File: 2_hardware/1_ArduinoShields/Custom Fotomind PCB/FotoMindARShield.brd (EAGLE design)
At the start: 160 x 100 mm, 22 parts

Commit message: Last lines PCB Shield
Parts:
- moved R3 26.5 mm to (17.1, 31.8)
- moved CAMERA 11.9 mm to (18.1, 8.26)
- moved R4 10.8 mm to (8.26, 8.89), turned to 270 degrees
- moved R7 9.94 mm to (45.1, 37.8), turned to 90 degrees
- moved LED1 8.89 mm to (11.4, 22.9)
- moved LED2 8.89 mm to (5.08, 22.9)
- moved R5 3.81 mm to (5.08, 8.89), turned to 270 degrees
- moved R6 2.54 mm to (61.0, 36.8)
- moved R2 1.59 mm to (48.3, 37.8)
- moved R1 1.00 mm to (51.1, 37.8)
- turned EXTSENSOR to 180 degrees
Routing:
- net N$8: track 0.00 -> 135.3 mm
- net N$7: track 7.62 -> 121.0 mm
- net N$30: track 0.00 -> 75.9 mm
- net N$19: track 27.6 -> 87.4 mm
- net N$1: track 0.00 -> 58.0 mm
- net N$15: track 0.00 -> 54.5 mm
- net N$21: track 21.9 -> 76.4 mm
- net GND: track 61.7 -> 110.2 mm
- net N$14: track 0.00 -> 46.7 mm
- net N$13: track 0.00 -> 46.4 mm
- net N$28: track 0.00 -> 28.6 mm
- net N$26: track 0.00 -> 24.8 mm
- net N$2: track 0.00 -> 20.6 mm
- net N$5: track 0.00 -> 13.9 mm
- net N$20: track 0.00 -> 9.88 mm
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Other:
- board size 160 x 100 mm -> 73.6 x 59.4 mm

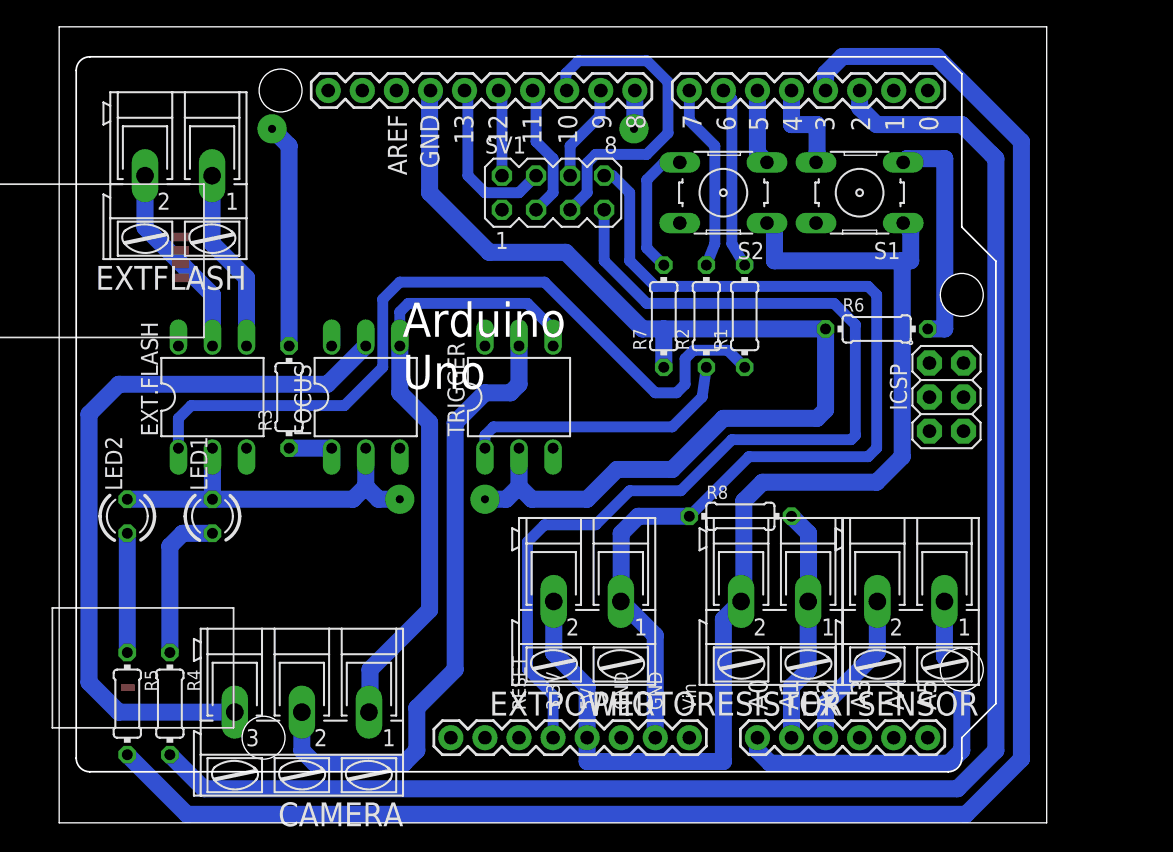
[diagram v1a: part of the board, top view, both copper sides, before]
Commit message: New ultrasonic feature
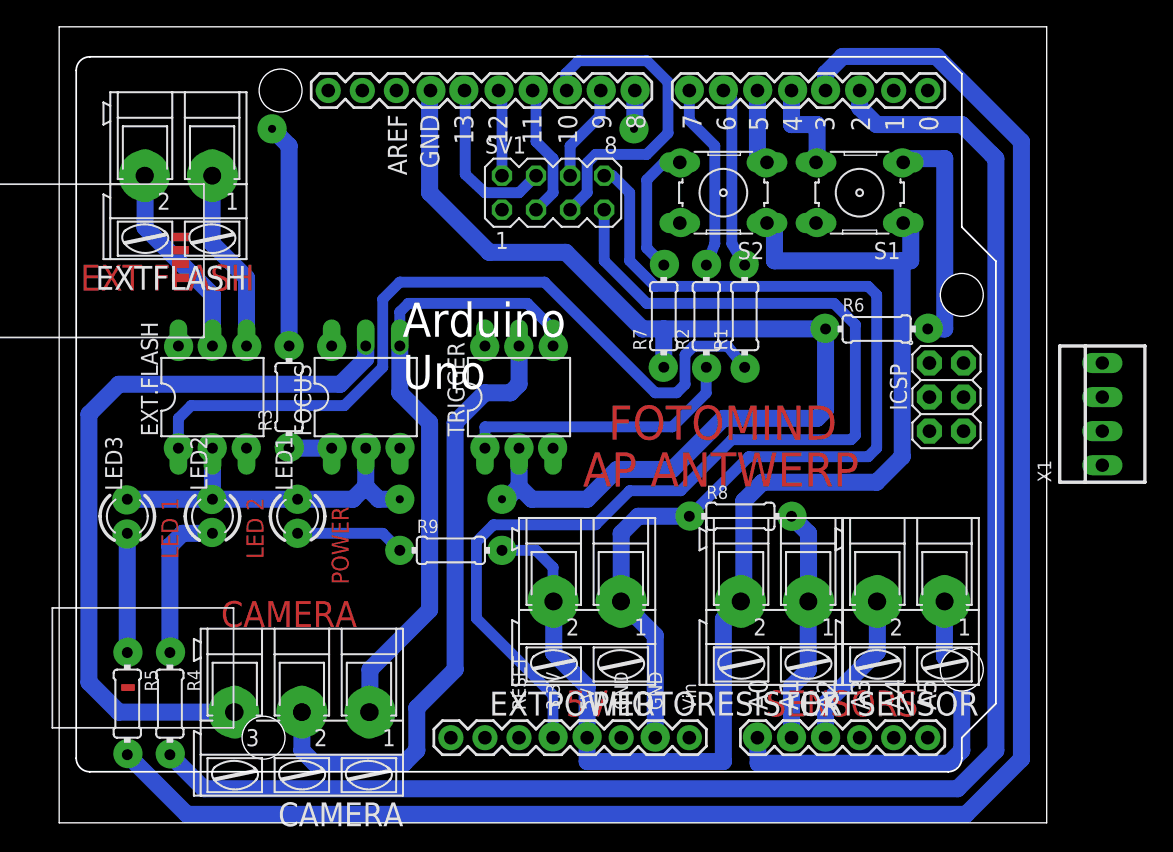
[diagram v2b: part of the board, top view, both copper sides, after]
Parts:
- added LED3: (no value), led:LED3MM
- added R9: 1k, eagle-ltspice:0204/7
- added X1: ULTRASOON, con-molex:22-23-2041
- S1: value (none) -> Trigger
- S2: value (none) -> Flash
- SV1: value (none) -> Wireless nRF24
- moved LED1 6.35 mm to (17.8, 22.9)
- moved LED2 6.35 mm to (11.4, 22.9)
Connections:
- removed net N$19: EXTPOWER.2, PCB1.5V, PHOTORESISTOR.2, S1.1, S2.1
- new net N$105: PCB1.0, X1.3
- new net N$107: PCB1.1, X1.2
- new net N$79: EXTPOWER.2, PCB1.5V, PHOTORESISTOR.2, R9.2, S1.1, S2.1, X1.4
- new net N$92: LED1.A, R9.1
- net GND: now also LED3.K
- net N$10: now also LED2.A; no longer LED1.A
- net N$21: now also X1.1
- net N$9: now also LED3.A; no longer LED2.A
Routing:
- net N$79: track 0.00 -> 94.4 mm, vias 0 -> 1
- net N$19: track 87.4 -> 0.00 mm, vias 0 -> 1
- net N$92: track 0.00 -> 8.15 mm
- net N$30: track 75.9 -> 81.3 mm
- net GND: track 110.2 -> 108.9 mm
- net N$28: track 28.6 -> 29.2 mm, vias 0 -> 1
- net N$15: track 54.5 -> 55.1 mm, vias 0 -> 1
- net N$1: track 58.0 -> 58.5 mm, vias 0 -> 1
- net N$2: track 20.6 -> 21.0 mm, vias 0 -> 1
- net N$8: vias 0 -> 1
- net N$6: vias 1 -> 2
- net N$21: vias 0 -> 1
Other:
- board text added: "5V"
- board text added: "AP ANTWERP"
- board text added: "CAMERA"
- board text added: "EXT FLASH"
- board text added: "FOTOMIND"
- board text added: "LED 1"
- board text added: "LED 2"
- board text added: "POWER"
- board text added: "SENSORS"

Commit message: Final PCB-design, ready to mill ! (+groundplane)
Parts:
- moved X1 3.00 mm to (75.2, 28.9), turned to 270 degrees
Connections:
- removed net N$107: PCB1.1, X1.2
- new net N$106: PCB1.0, X1.2
- net N$105: now also PCB1.1; no longer PCB1.0
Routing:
- net N$105: track 0.00 -> 38.3 mm
- net N$106: track 0.00 -> 32.7 mm
- net N$8: track 135.3 -> 143.7 mm
- net N$21: track 76.4 -> 83.4 mm, vias 1 -> 2
- net N$79: track 94.4 -> 101.2 mm
- net N$6: track 19.6 -> 24.2 mm
- net GND: track 108.9 -> 110.9 mm
- net N$7: track 121.0 -> 122.1 mm
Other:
- board size 73.6 x 59.4 mm -> 79.4 x 59.4 mm
- board text added: "FOTOMIND 2.0"
- board text removed: "FOTOMIND"
